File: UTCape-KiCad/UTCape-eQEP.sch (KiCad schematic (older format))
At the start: 2 parts

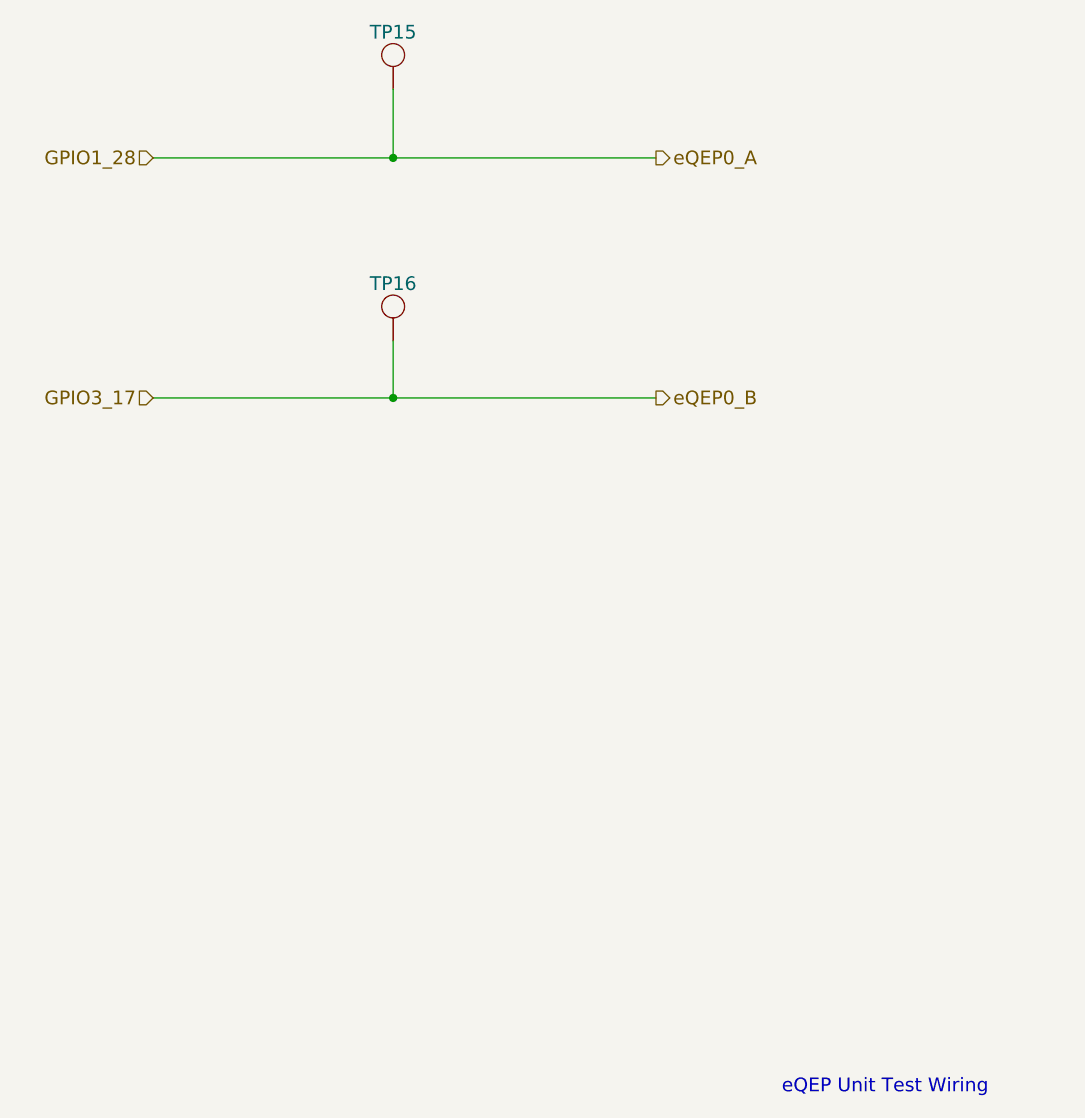
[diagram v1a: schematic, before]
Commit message: added missing resistor in divider plus some protection resistors, regenerated fab files
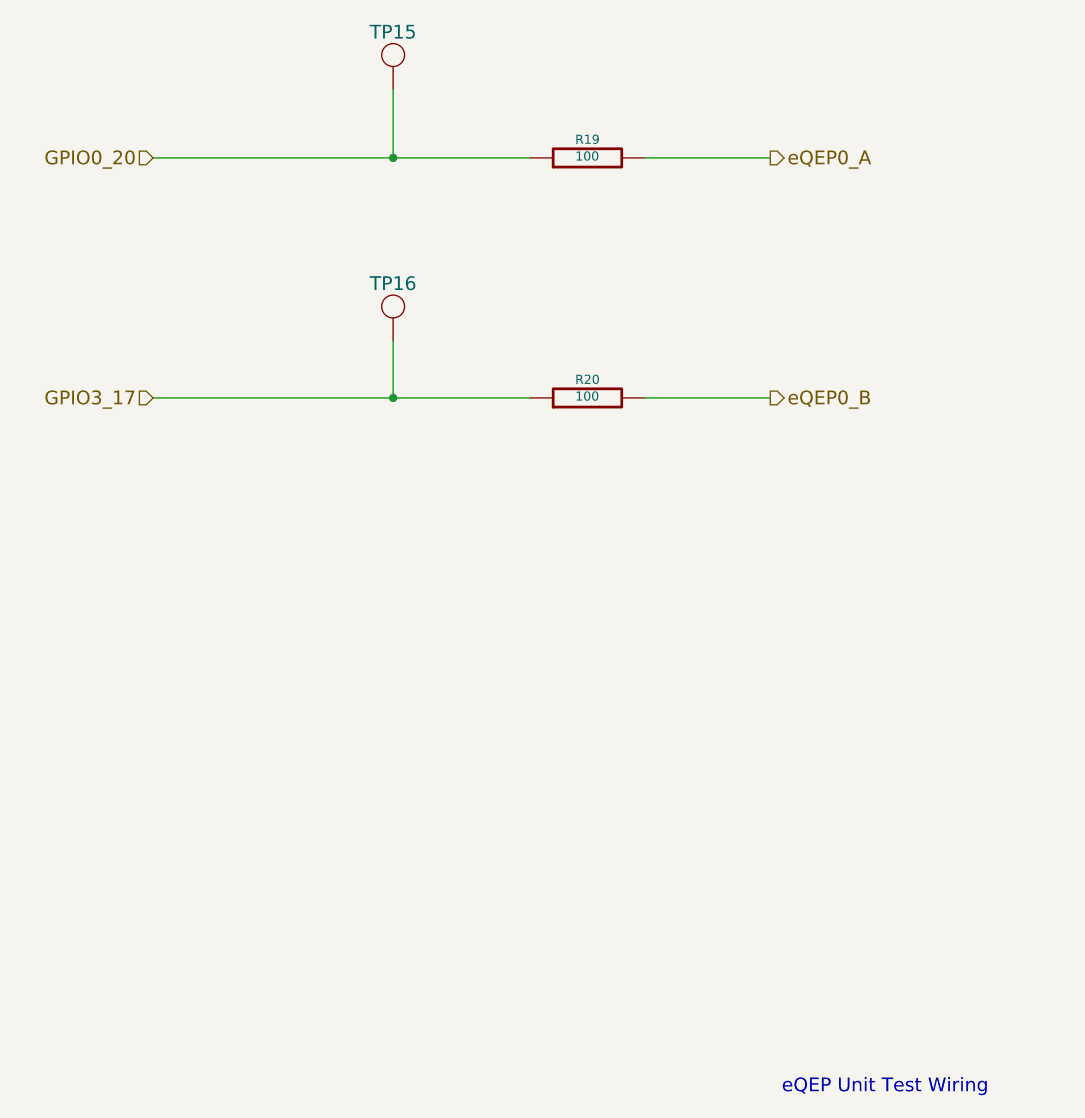
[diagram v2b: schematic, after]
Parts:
- added R19, R20: 100, ~, symbol R
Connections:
- net GPIO3_17: now also R20.1
- net GPIO1_28 renamed GPIO0_20
- net GPIO0_20: now also R19.1
- new net eQEP0_A: R19.2
- new net eQEP0_B: R20.2
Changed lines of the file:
@@
 Sheet 9 9
 Title ""
-Date "24 feb 2015"
+Date "24 mar 2015"
 Rev ""
 Comp ""
@@
 Comment4 ""
 $EndDescr
-Text HLabel 6800 3450 2    60   Output ~ 0
+Text HLabel 7300 3450 2    60   Output ~ 0
 eQEP0_A
-Text HLabel 6800 4500 2    60   Output ~ 0
+Text HLabel 7300 4500 2    60   Output ~ 0
 eQEP0_B
-Text HLabel 4600 3450 0    60   Input ~ 0
-GPIO1_28
 Text HLabel 4600 4500 0    60   Input ~ 0
 GPIO3_17
 Wire Wire Line
-	4600 3450 6800 3450
-Wire Wire Line
-	4600 4500 6800 4500
+	4600 4500 6250 4500
 $Comp
 L TEST_POINT TP15
@@
 $EndComp
 Wire Wire Line
-	5650 3150 5650 3450
+	5650 3450 5650 3150
 Connection ~ 5650 3450
 Wire Wire Line
-	5650 4250 5650 4500
+	5650 4500 5650 4250
 Connection ~ 5650 4500
 Text Notes 7350 7550 0    60   ~ 0
@@
 03 43 83 61 8C 09 03 03 03 03 43 83 61 8C 09 03 03 03 03 43 83 61 8C 09 03 03 03 03 43 83 61 03
 60 D2 64 32 30 30 30 30 34 84 CF 1C 00 A9 00 9C 01 A8 8B 59 19 06 06 06 06 06 E9 E3 33 80 C5 FF
-07 47 25 A5 D2 E9 03 52 D8 00 00 00 00 49 45 4E 44 AE 42 60 82 4A $EndBitmap
+07 47 25 A5 D2 E9 03 52 D8 00 00 00 00 49 45 4E 44 AE 42 60 82 CF $EndBitmap
 EndData
 $EndBitmap
+$Comp
+L R R19
+U 1 1 54F66AB7
+P 6500 3450
+F 0 "R19" V 6580 3450 40  0000 C CNN
+F 1 "100" V 6507 3451 40  0000 C CNN
+F 2 "~" V 6430 3450 30  0000 C CNN
+F 3 "~" H 6500 3450 30  0000 C CNN
+	1    6500 3450
+	0    -1   -1   0
+$EndComp
+$Comp
+L R R20
+U 1 1 54F66AD3
+P 6500 4500
+F 0 "R20" V 6580 4500 40  0000 C CNN
+F 1 "100" V 6507 4501 40  0000 C CNN
+F 2 "~" V 6430 4500 30  0000 C CNN
+F 3 "~" H 6500 4500 30  0000 C CNN
+	1    6500 4500
+	0    -1   -1   0
+$EndComp
+Wire Wire Line
+	6750 4500 7300 4500
+Wire Wire Line
+	6750 3450 7300 3450
+Text HLabel 4600 3450 0    60   Input ~ 0
+GPIO0_20
+Wire Wire Line
+	4600 3450 6250 3450
 $EndSCHEMATC
